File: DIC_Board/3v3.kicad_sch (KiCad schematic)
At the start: 8 parts, among them J30 0430450200, U30 TPS27S100APWPR

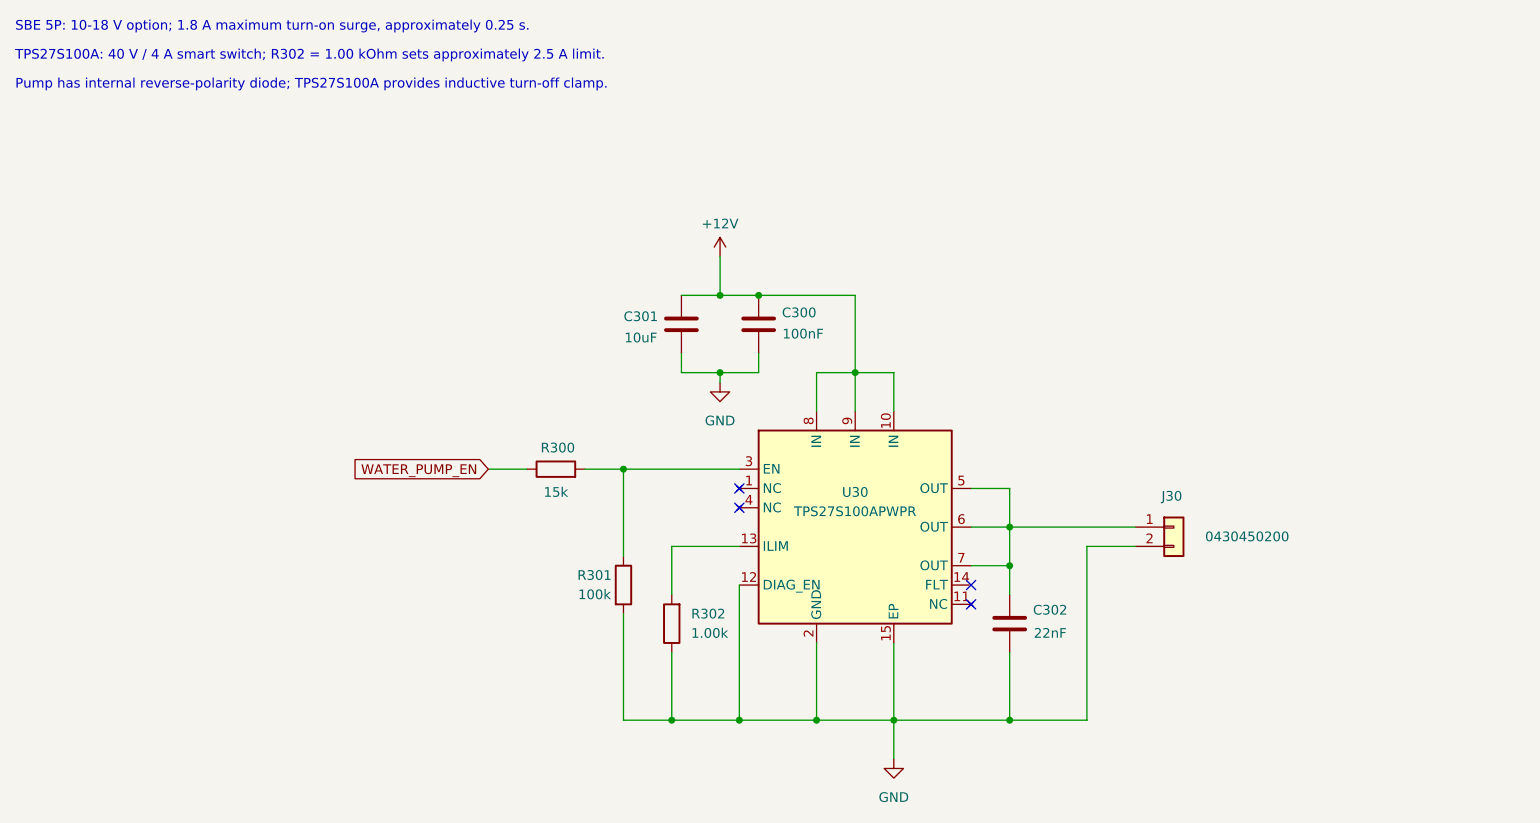
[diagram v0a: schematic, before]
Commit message: Separated the power sheets, did the sensor sheets.
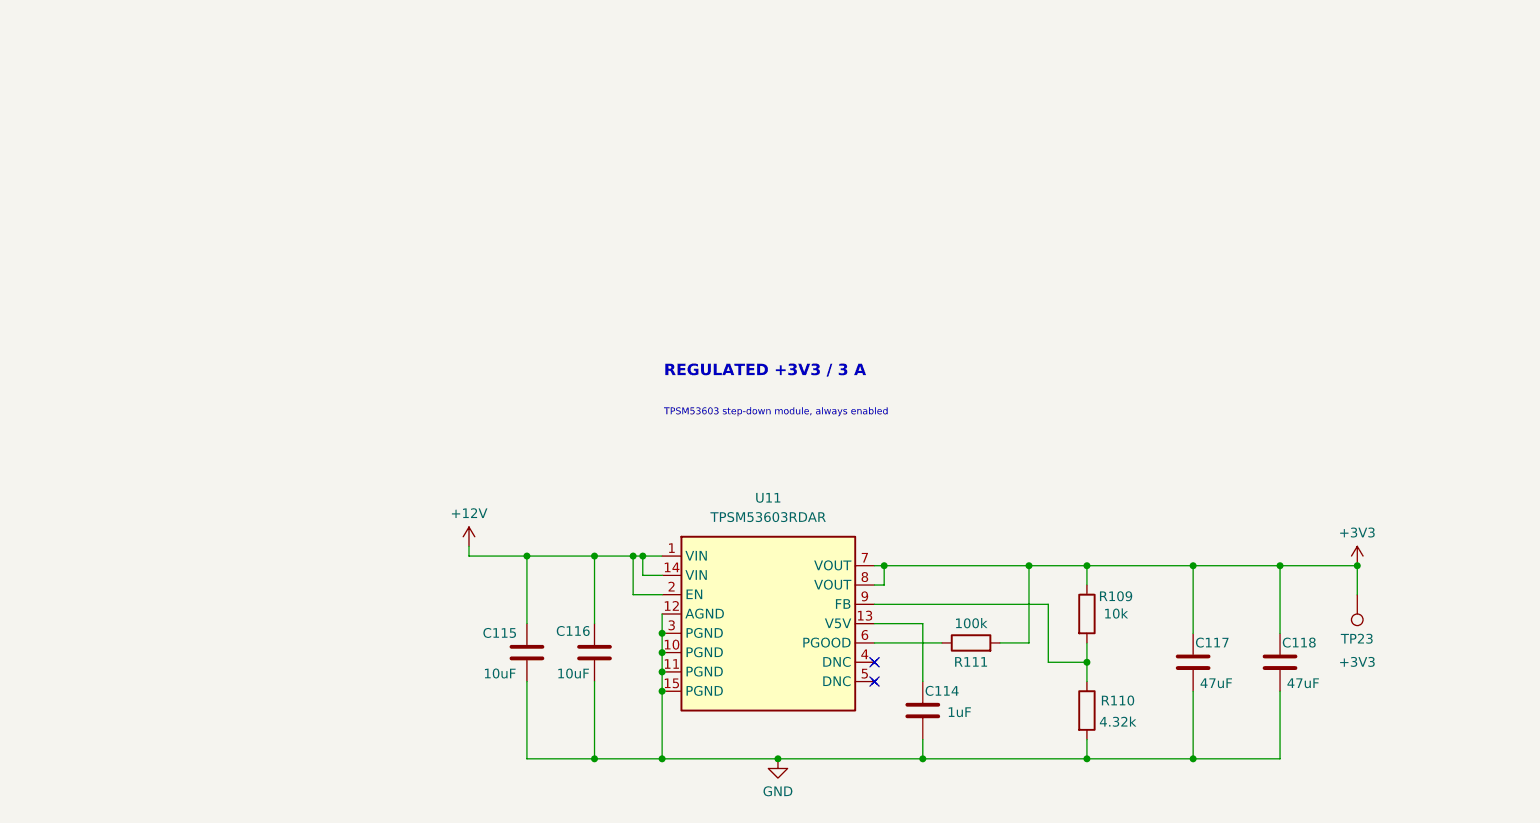
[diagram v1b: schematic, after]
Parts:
- removed C300: 100nF, Capacitor_SMD:C_0402_1005Metric, symbol Device:C
- removed C301: 10uF, Capacitor_SMD:C_1206_3216Metric, symbol Device:C
- removed C302: 22nF, Capacitor_SMD:C_0402_1005Metric, symbol Device:C
- removed J30: 0430450200, Connector_Molex:Molex_Micro-Fit_3.0_43045-0200_2x01_P3.00mm_Horizontal, symbol Connector_Generic:Conn_01x02
- removed R300: 15k, Resistor_SMD:R_0402_1005Metric, symbol Device:R
- removed R301: 100k, Resistor_SMD:R_0402_1005Metric, symbol Device:R
- removed R302: 1.00k, Resistor_SMD:R_0402_1005Metric, symbol Device:R
- removed U30: TPS27S100APWPR, Package_SO:Texas_HTSSOP-14-1EP_4.4x5mm_P0.65mm_EP3.4x5mm_Mask3.155x3.255mm_ThermalVias, symbol DIC_Board:TPS27S100A
- added C114: 1uF, Capacitor_SMD:C_0603_1608Metric, symbol Device:C
- added C115, C116: 10uF, Capacitor_SMD:C_1206_3216Metric, symbol Device:C
- added C117, C118: 47uF, Capacitor_SMD:C_1210_3225Metric, symbol Device:C
- added R109: 10k, Resistor_SMD:R_0402_1005Metric, symbol Device:R
- added R110: 4.32k, Resistor_SMD:R_0402_1005Metric, symbol Device:R
- added R111: 100k, Resistor_SMD:R_0402_1005Metric, symbol Device:R
- added TP23: +3V3, TestPoint:TestPoint_Plated_Hole_D2.0mm, symbol Connector:TestPoint
- added U11: TPSM53603RDAR, Package_DFN_QFN:Texas_B3QFN-14-1EP_5x5.5mm_P0.65mm_ThermalVia, symbol DIC_Board:TPSM53603RDA
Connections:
- net +12V: now also C115.1, C116.1, U11.1 (VIN), U11.14 (VIN), U11.2 (EN)
- net GND: now also C114.2, C115.2, C116.2, C117.2, C118.2, R110.2, U11.10 (PGND), U11.11 (PGND), U11.12 (AGND), U11.15 (PGND), U11.3 (PGND)
- new net: R109.2, R110.1, U11.9 (FB)
- new net: R111.1, U11.6 (PGOOD)
- new net: C114.1, U11.13 (V5V)
- new net +3V3: C117.1, C118.1, R109.1, R111.2, TP23.1, U11.7 (VOUT), U11.8 (VOUT)
- no-connect marks 4 -> 2
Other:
- note added: "REGULATED +3V3 / 3 A"
- note added: "TPSM53603 step-down module, always enabled"
- note removed: "Pump has internal reverse-polarity diode; TPS27S100A provides inductive turn-off clamp."
- note removed: "SBE 5P: 10-18 V option; 1.8 A maximum turn-on surge, approximately 0.25 s."
- note removed: "TPS27S100A: 40 V / 4 A smart switch; R302 = 1.00 kOhm sets approximately 2.5 A limit."
- title: Water Pump -> (none)

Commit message: Synchronize schematic hierarchy and MCU pin map
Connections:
- net +12V renamed P_IN
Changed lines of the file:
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@@
+		)
+	)
+	(hierarchical_label "P_IN"
+		(shape input)
+		(at 88.9 91.44 90)
+		(effects
+			(font
+				(size 1.27 1.27)
+			)
+			(justify left)
 		)
 	)
@@
 					(unit 1)
 				)
-			)
-		)
-	)
-	(symbol
-		(lib_id "power:+12V")
-		(at 88.9 91.44 0)
-		(unit 1)
-		(body_style 1)
-		(exclude_from_sim no)
-		(in_bom yes)
-		(on_board yes)
-		(in_pos_files yes)
-		(dnp no)
-		(property "Reference" "#PWR0108"
-			(at 91.44 88.9 0)
-			(hide yes)
-			(show_name no)
-			(do_not_autoplace no)
-			(effects
-				(font
-					(size 1.27 1.27)
-				)
-			)
-		)
-		(property "Value" "+12V"
-			(at 88.9 87.122 0)
-			(show_name no)
-			(do_not_autoplace no)
-			(effects
-				(font
-					(size 1.27 1.27)
-				)
-			)
-		)
-		(property "Footprint" ""
-			(at 88.9 91.44 0)
-			(hide yes)
-			(show_name no)
-			(do_not_autoplace no)
-			(effects
-				(font
-					(size 1.27 1.27)
-				)
-			)
-		)
-		(property "Datasheet" ""
-			(at 88.9 91.44 0)
-			(hide yes)
-			(show_name no)
-			(do_not_autoplace no)
-			(effects
-				(font
-					(size 1.27 1.27)
-				)
-			)
-		)
-		(property "Description" ""
-			(at 88.9 91.44 0)
-			(hide yes)
-			(show_name no)
-			(do_not_autoplace no)
-			(effects
-				(font
-					(size 1.27 1.27)
-				)
-			)
-		)
-		(pin "1"
-		)
-		(instances
-			(project "DIC_Board"
-				(path "/bb0ef0df-c181-443a-843c-695cd2e0efee/b7e0d3a1-6a4d-4d5e-9f2b-31c8a7d64e20/2161909f-1018-4cef-9d4b-129c48d3907b"
-					(reference "#PWR0108")
-					(unit 1)
-				)

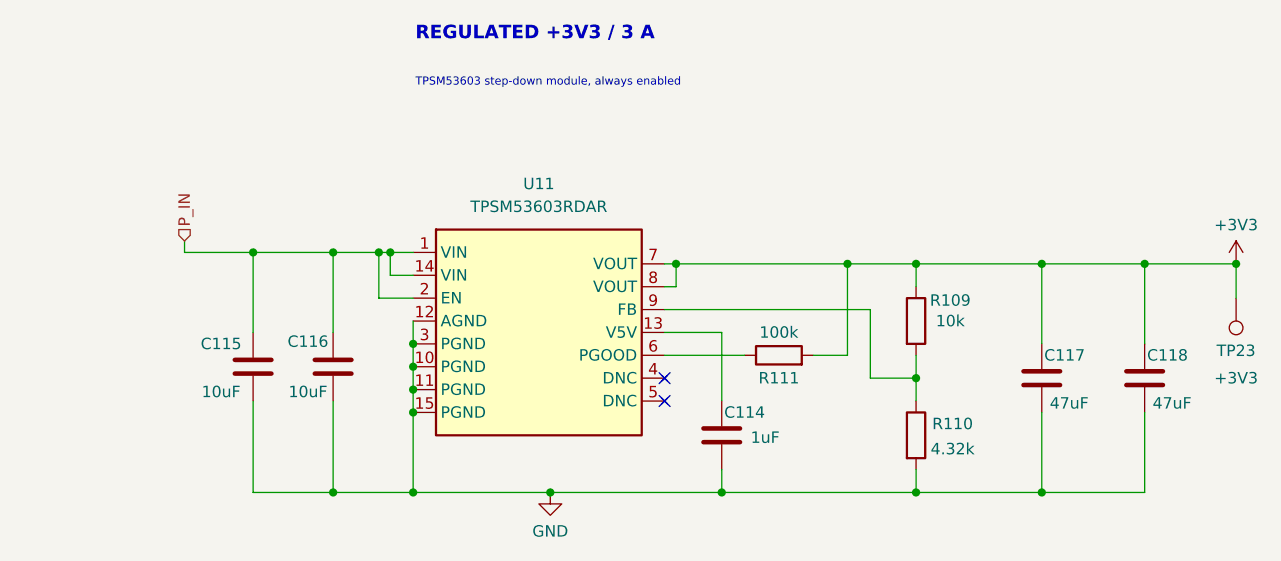
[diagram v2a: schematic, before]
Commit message: Synchronize power, communications, and MCU configuration
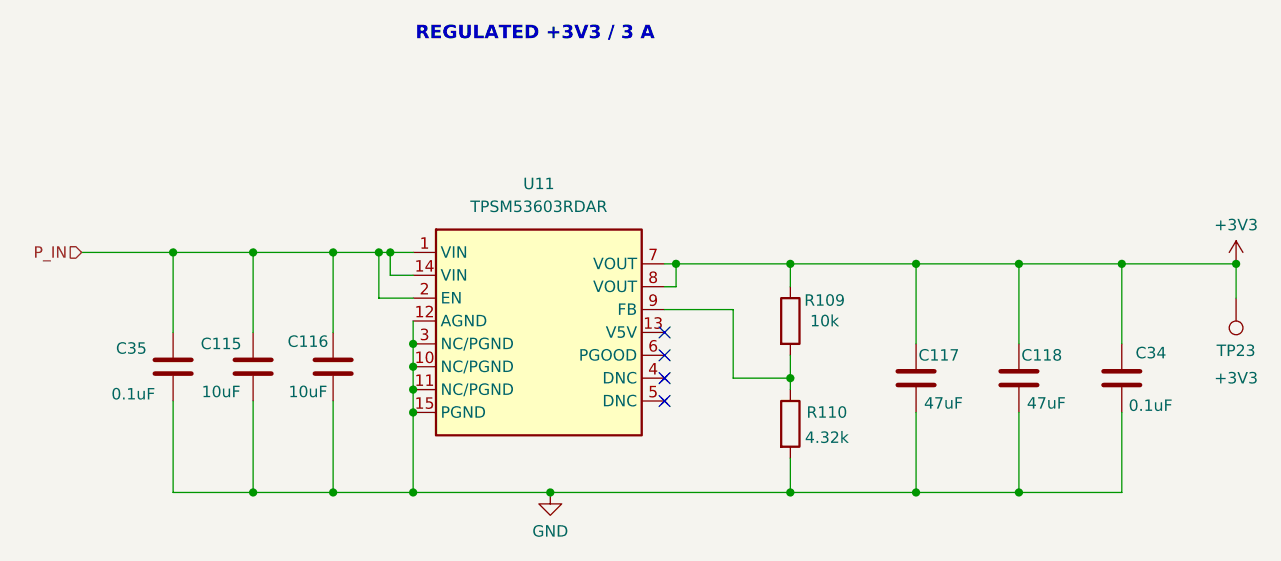
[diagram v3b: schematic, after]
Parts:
- removed C114: 1uF, Capacitor_SMD:C_0603_1608Metric, symbol Device:C
- removed R111: 100k, Resistor_SMD:R_0402_1005Metric, symbol Device:R
- added C34, C35: 0.1uF, symbol Device:C
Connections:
- net +3V3: now also C34.1
- net GND: now also C34.2, C35.2
- net P_IN: now also C35.1
- no-connect marks 2 -> 4
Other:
- note removed: "TPSM53603 step-down module, always enabled"
- moved on the sheet: C117, C118, R109, R110

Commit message: Updated board for layout! All footprints added
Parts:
- added C901: 180uF 16V, Capacitor_SMD:CP_Elec_6.3x5.9, symbol Device:C_Polarized
- C34, C35: footprint (none) -> Capacitor_SMD:C_0603_1608Metric; BOM Source (none) -> https://product.tdk.com/en/search/capacitor/ceramic/mlcc/in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; Dielectric (none) -> X7R; MPN (none) -> C1608X7R1H104K080AA; Manufacturer (none) -> TDK; Tolerance (none) -> 10%; Voltage Rating (none) -> 50V
- TP23: now left out of the parts list
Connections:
- net +3V3: now also C901.1
- net GND: now also C901.2
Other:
- note added: "Output bulk"
- moved on the sheet: TP23

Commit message: Let gpt6 astra have a go at routing. bad results.
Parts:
- TP23: footprint TestPoint:TestPoint_Plated_Hole_D2.0mm -> TestPoint:TestPoint_Pad_D1.0mm
- U11: footprint Package_DFN_QFN:Texas_B3QFN-14-1EP_5x5.5mm_P0.65mm_ThermalVia -> DIC_Board:TPSM53603_Thermal_Drill0p3
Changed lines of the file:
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@@
 			)
 		)
-		(property "Footprint" "TestPoint:TestPoint_Plated_Hole_D2.0mm"
+		(property "Footprint" "TestPoint:TestPoint_Pad_D1.0mm"
 			(at 224.79 97.79 0)
 			(hide yes)
@@
 			)
 		)
-		(property "Footprint" "Package_DFN_QFN:Texas_B3QFN-14-1EP_5x5.5mm_P0.65mm_ThermalVia"
+		(property "Footprint" "DIC_Board:TPSM53603_Thermal_Drill0p3"
 			(at 128.27 101.6 0)
 			(hide yes)
